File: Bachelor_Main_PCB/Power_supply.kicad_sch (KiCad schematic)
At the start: 22 parts, among them IC1 LD3985M18R, U10 LMR51450FNDRRR, U9 LM73100RPWR

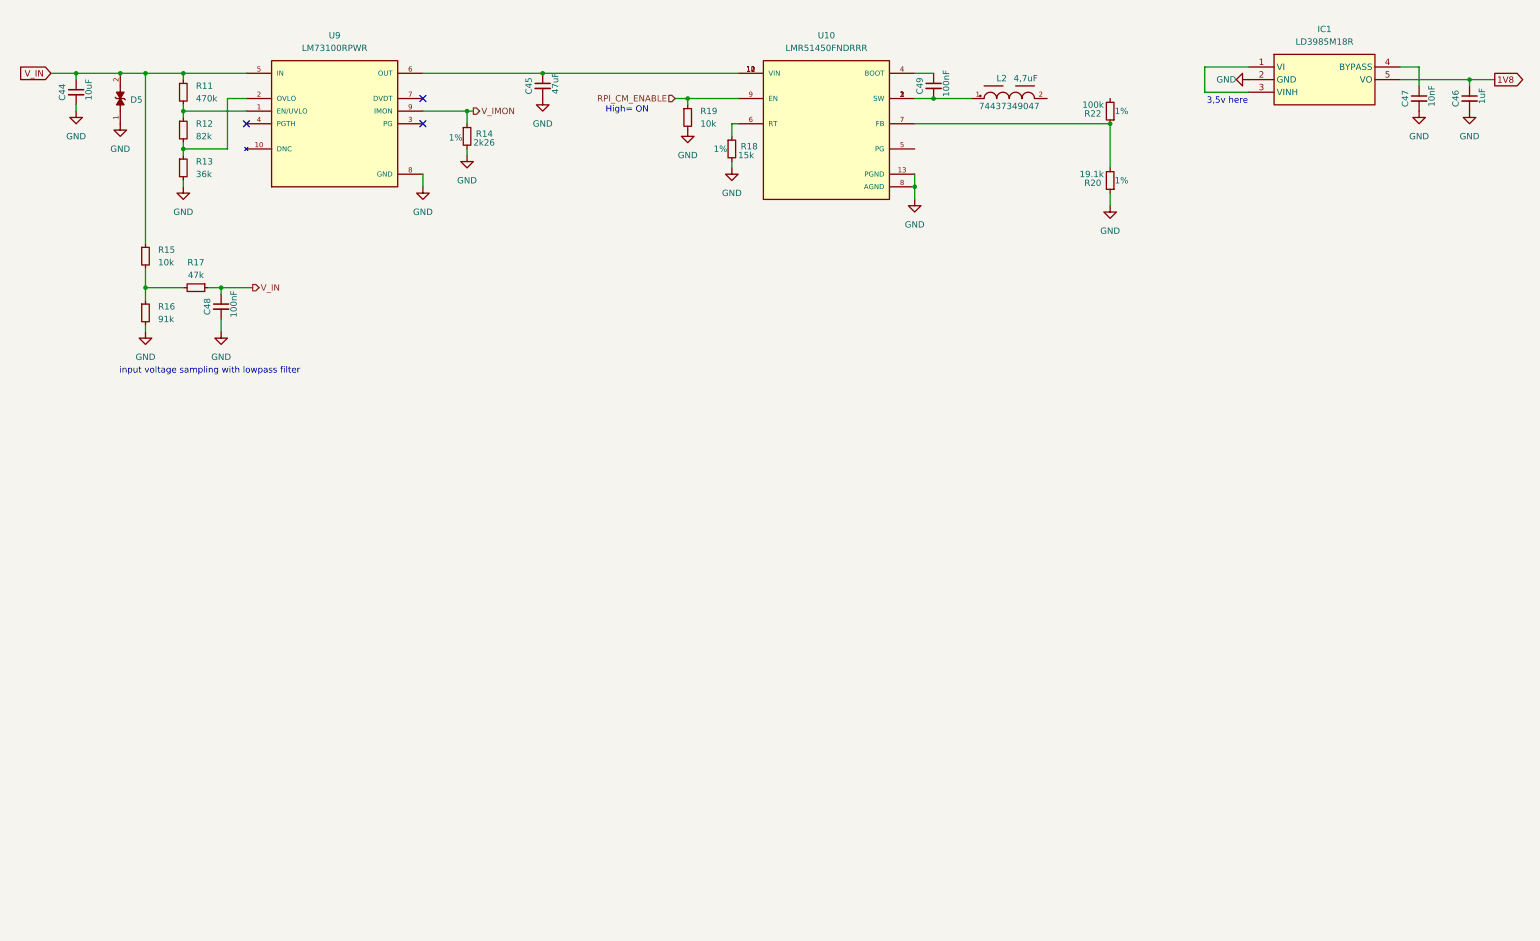
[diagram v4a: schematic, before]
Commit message: add 3,3uH inductor for 3,5v and add Rff and Cff to FB pin
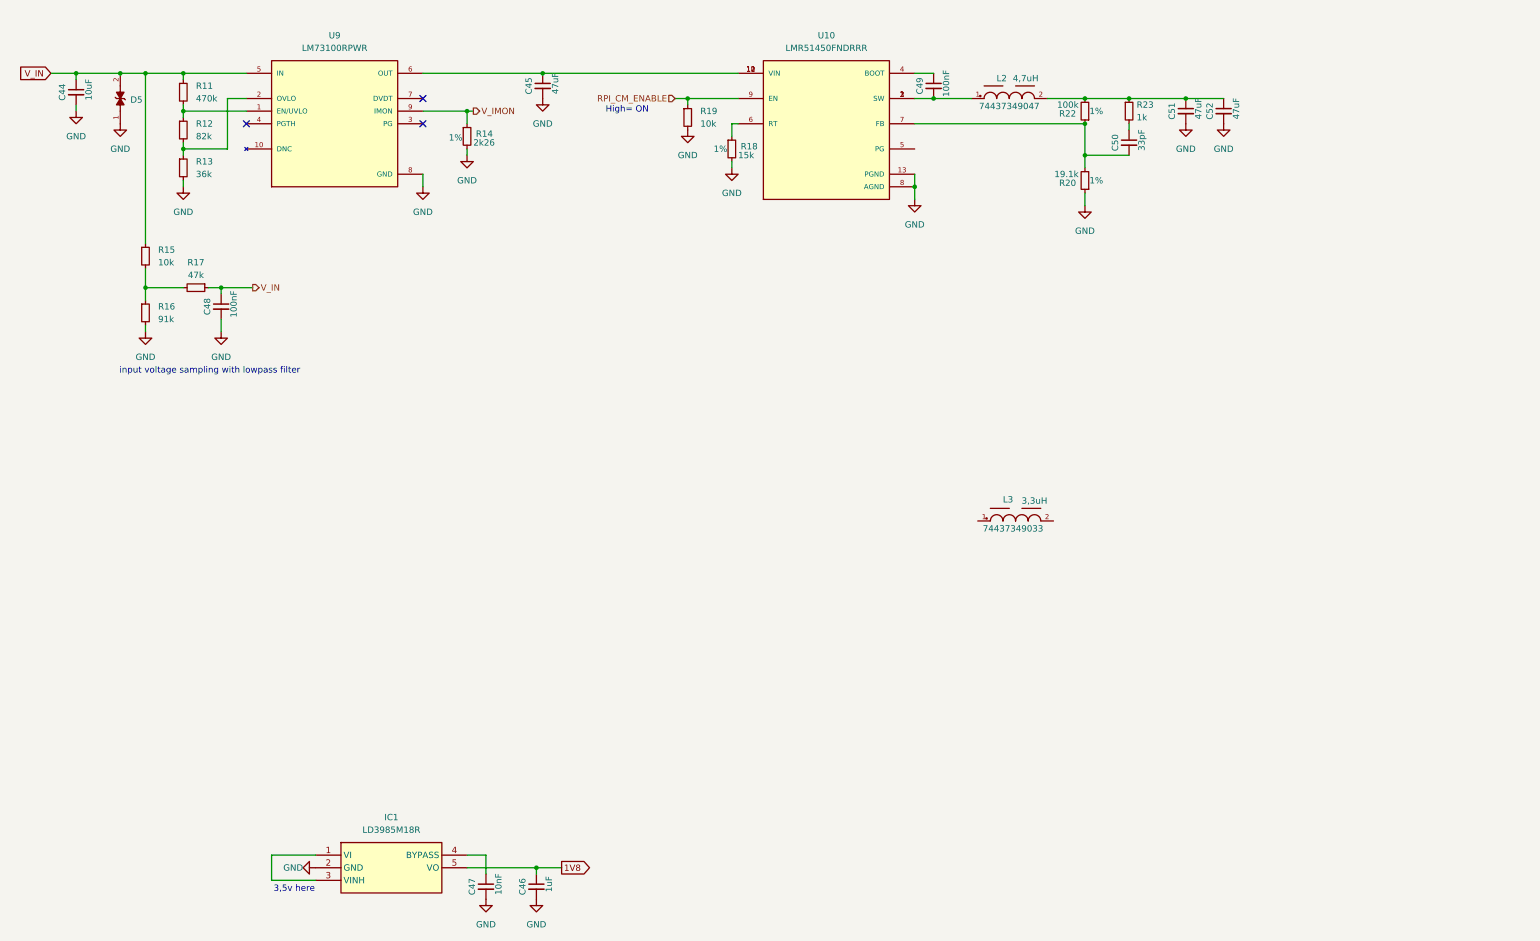
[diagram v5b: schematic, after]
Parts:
- added C50: 33pF, Capacitor_SMD:C_0603_1608Metric, symbol Device:C_Small
- added C51, C52: 47uF, Capacitor_SMD:C_0603_1608Metric, symbol Device:C_Small
- added L3: 3,3uH, WE-LHMI_7050:WE-LHMI_7050, symbol WE-LHMI_7050_3uH3:WE-LHMI_7050
- added R23: 1k, Resistor_SMD:R_0402_1005Metric, symbol Device:R_Small
- L2: value 4,7uF -> 4,7uH
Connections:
- net GND: now also C51.2, C52.2
- net at L2.2: now also R22.2, C51.1, C52.1, R23.1
- net at R20.2, R22.1, U10.7 (FB): now also C50.2
- new net: C50.1, R23.2
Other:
- moved on the sheet: C46, C47, IC1, R20, R22

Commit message: Add series inductors to switch mode convertors. Add screw terminal
For the audiomoth power.
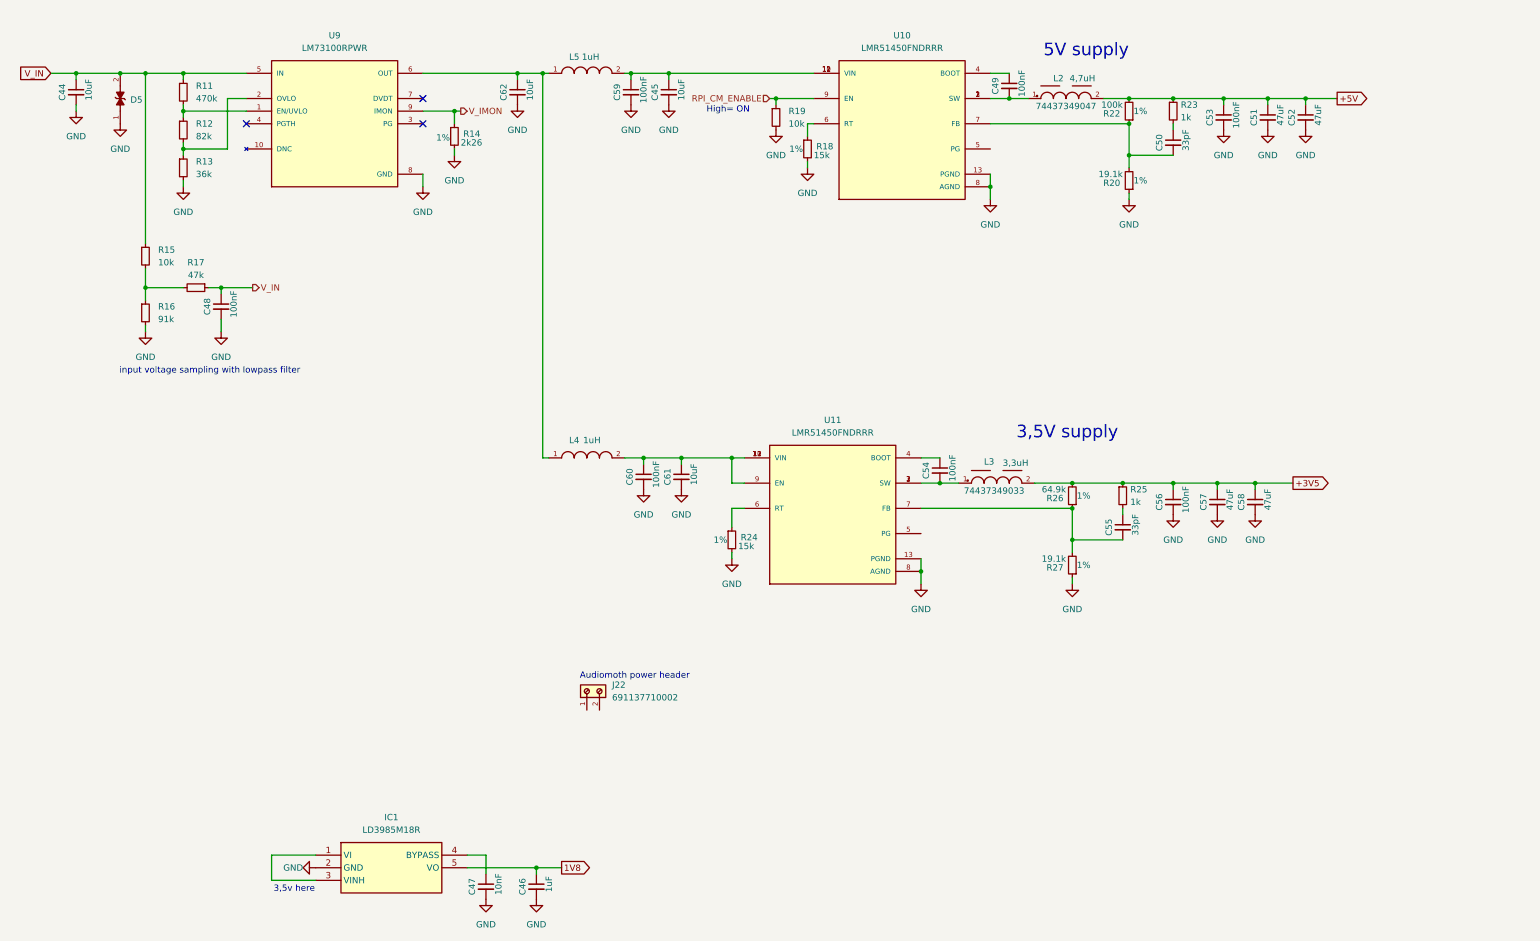
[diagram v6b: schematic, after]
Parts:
- added C53, C54, C56, C59, C60: 100nF, Capacitor_SMD:C_0603_1608Metric, symbol Device:C_Small
- added C55: 33pF, Capacitor_SMD:C_0603_1608Metric, symbol Device:C_Small
- added C57, C58: 47uF, Capacitor_SMD:C_0603_1608Metric, symbol Device:C_Small
- added C61, C62: 10uF, Capacitor_SMD:C_0603_1608Metric, symbol Device:C_Small
- added J22: 691137710002, 691137710002:691137710002, symbol 691137710002:691137710002
- added L4, L5: 1uH, LQM2HPN1R0MJHL:INDC2520X120N, symbol LQM2HPN1R0MJHL:LQM2HPN1R0MJHL
- added R24: 15k, Resistor_SMD:R_0402_1005Metric, symbol Device:R_Small
- added R25: 1k, Resistor_SMD:R_0402_1005Metric, symbol Device:R_Small
- added R26: 64.9k, Resistor_SMD:R_0402_1005Metric, symbol Device:R_Small
- added R27: 19.1k, Resistor_SMD:R_0402_1005Metric, symbol Device:R_Small
- added U11: LMR51450FNDRRR, LMR51450FNDRRR:CONV_LMR51450FNDRRR, symbol LMR51450FNDRRR:LMR51450FNDRRR
- C45: value 47uF -> 10uF
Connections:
- net GND: now also C53.2, C56.2, C57.2, C58.2, C59.2, C60.2, C61.2, C62.2, R24.2, R27.1, U11.13 (PGND), U11.8 (AGND)
- net +5V: now reaches C51.1, C52.1, L2.2, R22.2, R23.1
- net +5V: now also C53.1
- net at C45.1, U10.10 (VIN), U10.11 (VIN)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: now also C59.1, L5.2; no longer U9.6 (OUT)
- net at L3.1: now also C54.2, U11.1 (SW), U11.2 (SW), U11.3 (SW)
- net +3V5: now reaches L3.2
- net +3V5: now also C56.1, C57.1, C58.1, R25.1, R26.2
- new net: C54.1, U11.4 (BOOT)
- new net: C62.1, L4.1, L5.1, U9.6 (OUT)
- new net: C60.1, C61.1, L4.2, U11.10 (VIN), U11.11 (VIN), U11.12 (VIN), U11.9 (EN)
- new net: C55.2, R26.1, R27.2, U11.7 (FB)
- new net: C55.1, R25.2
- new net: R24.1, U11.6 (RT)
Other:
- note added: "3,5V supply"
- note added: "5V supply"
- note added: "Audiomoth power header"
- moved on the sheet: C45, C49, C50, C51, C52, L2, L3, R14, R18, R19, R20, R22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

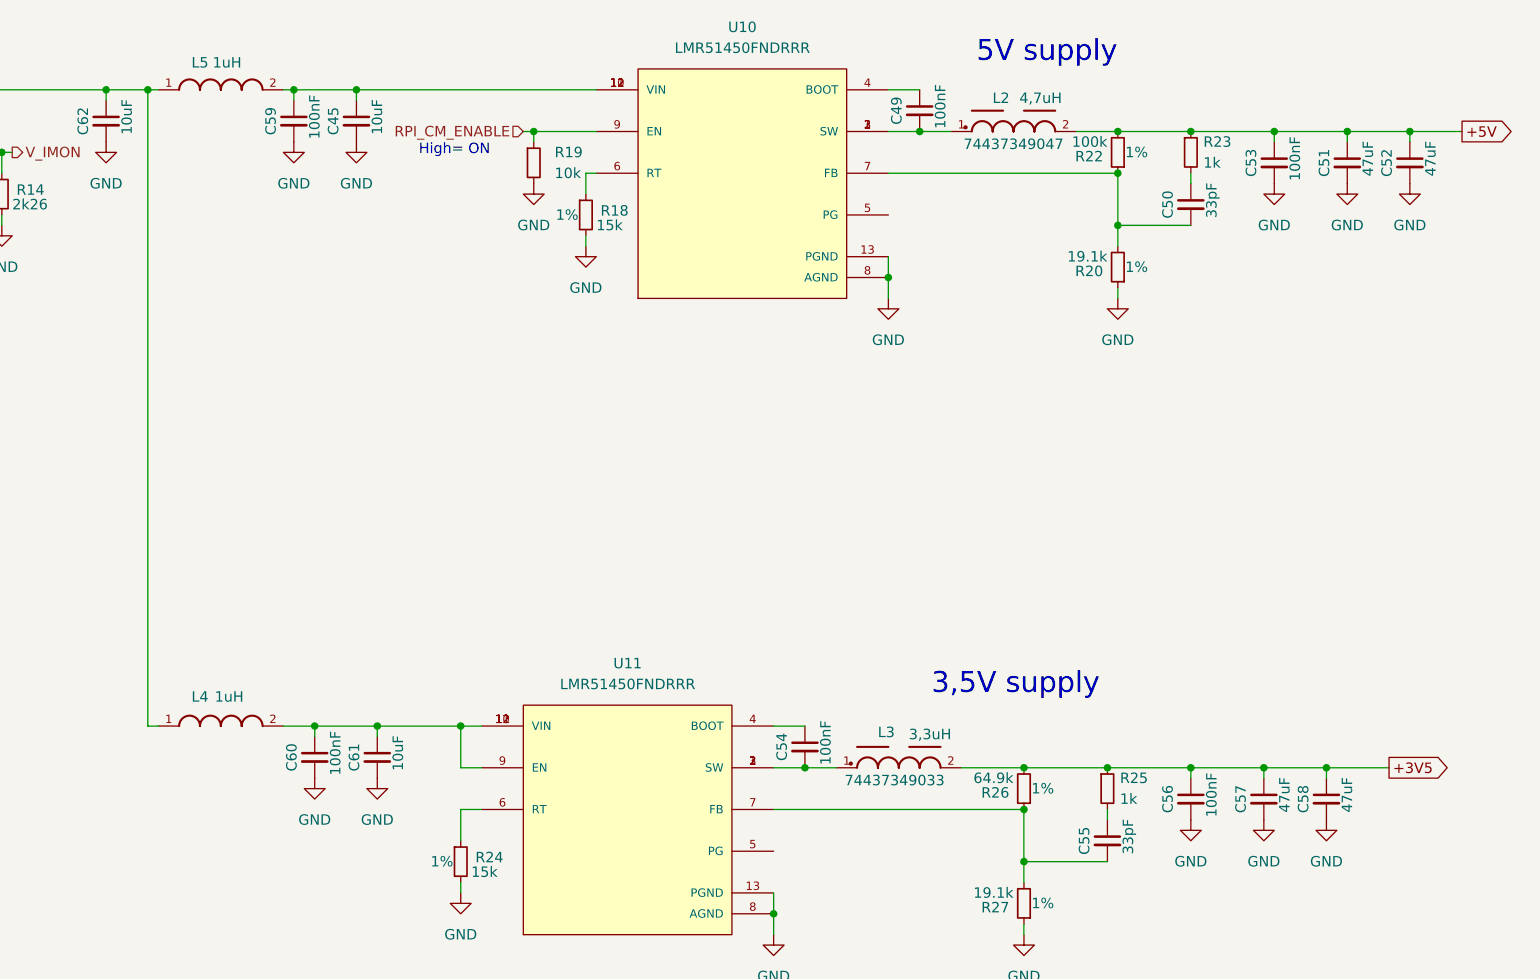
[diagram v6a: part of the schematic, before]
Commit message: Reinstated Mosfet RPI_CM_ENABLE controll
instead of enable pin on switch mode controller. this way the audiomoth can use the 5v supply with the capacitor multiplier.
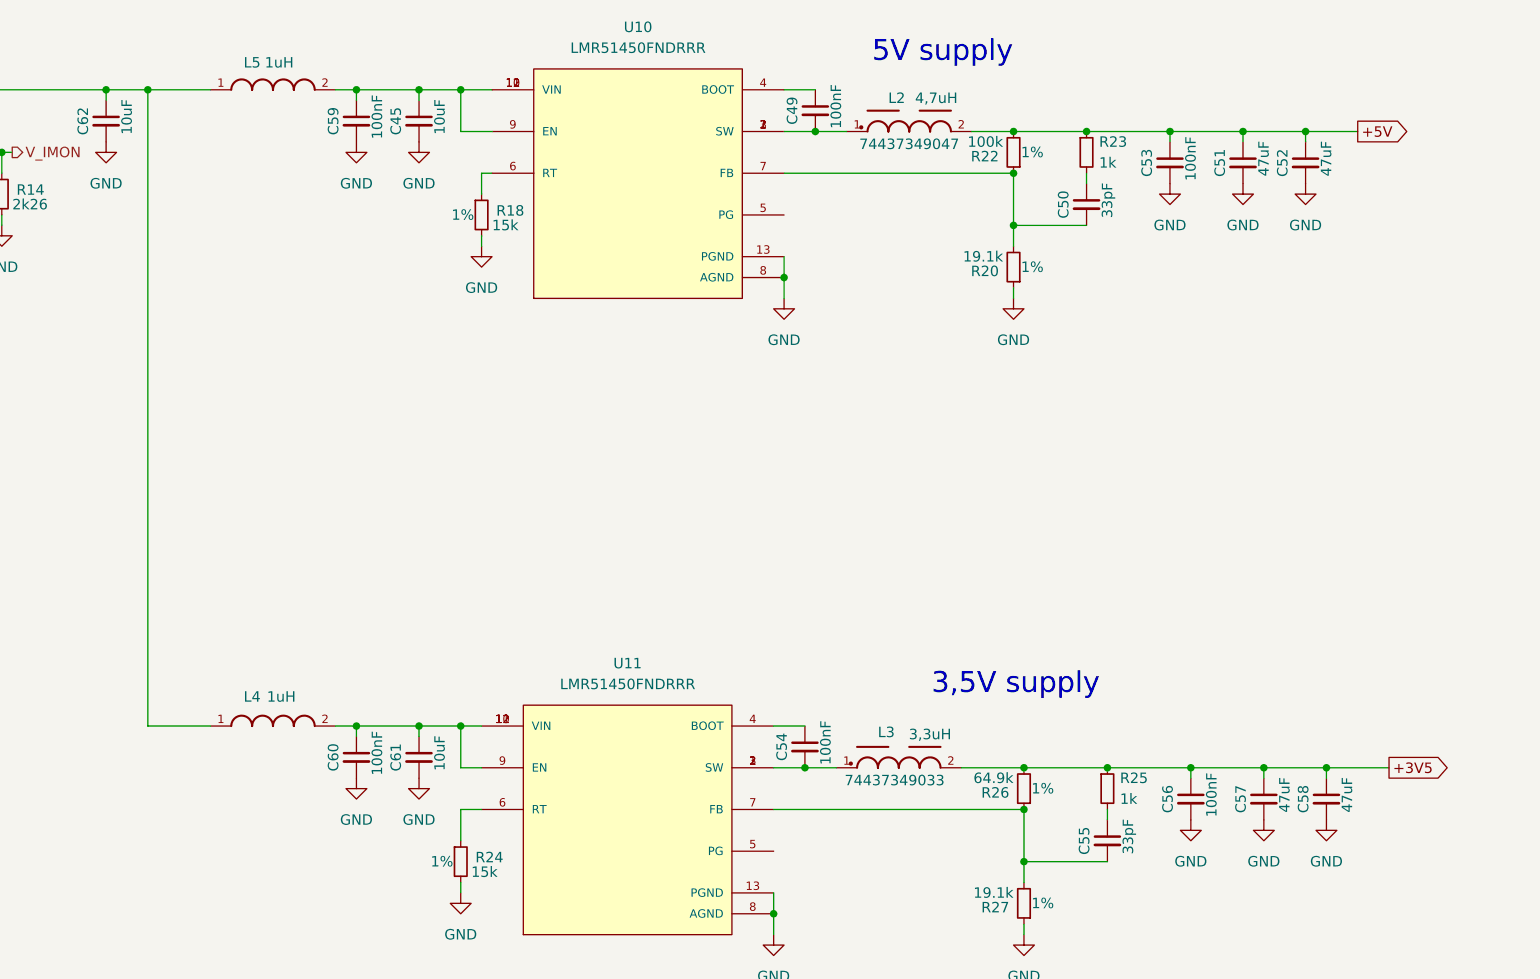
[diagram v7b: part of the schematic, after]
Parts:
- removed R19: 10k, Resistor_SMD:R_0402_1005Metric, symbol Device:R_Small
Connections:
- net RPI_CM_ENABLE is gone; now on an unnamed net: U10.9 (EN)
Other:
- note removed: "High= ON"
- moved on the sheet: C45, C49, C50, C51, C52, C53, C59, C60, C61, L2, L4, L5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
